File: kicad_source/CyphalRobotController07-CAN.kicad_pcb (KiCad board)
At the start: 2 copper layers, 140 x 70 mm, 177 parts, among them J1 BM04B-SRSS-TB, J10 x, J11 PowerPole, J12 Conn_01x02, J13 Conn_01x02, J14 Conn_01x02, J15 PinHeader_1x04, J16 PinHeader_1x04, J17 PinHeader_1x05, J18 Conn_01x02, J19 S6B-XH-A, J2 RASPBERRYPI_PICO, J20 S6B-XH-A, J3 BM04B-SRSS-TB, J4 B3B-PH-SM4-TB, J5 BM04B-GHS-TBT, J6 BM04B-GHS-TBT, J7 x, J8 x, J9 x, Q1 2N7002, Q2 IPD90P03P4L- 04, SW1 PTS636 SM43 SMTR LFS, U1 24LC64-I/SN, U10 ADS1015IDGS, U11 OPA2374AIDCN, U12 INA226, U13 IFX91041EFJ, U14 ITS4200S-ME-P, U15 ITS4200S-ME-P, U16 BNO085, U17 SN74LVC2T45DCUR, U18 SN74LVC2T45DCUR, U2 MCP2515-I/SO, U3 SN65HVD232, U4 74xx08, U5 IFX007T, U6 IFX007T, U7 IFX007T, U8 IFX007T, U9 OPA2374AIDCN, Y1 RH100-16.000-16-3030-EXT-TR, Y2 DNI

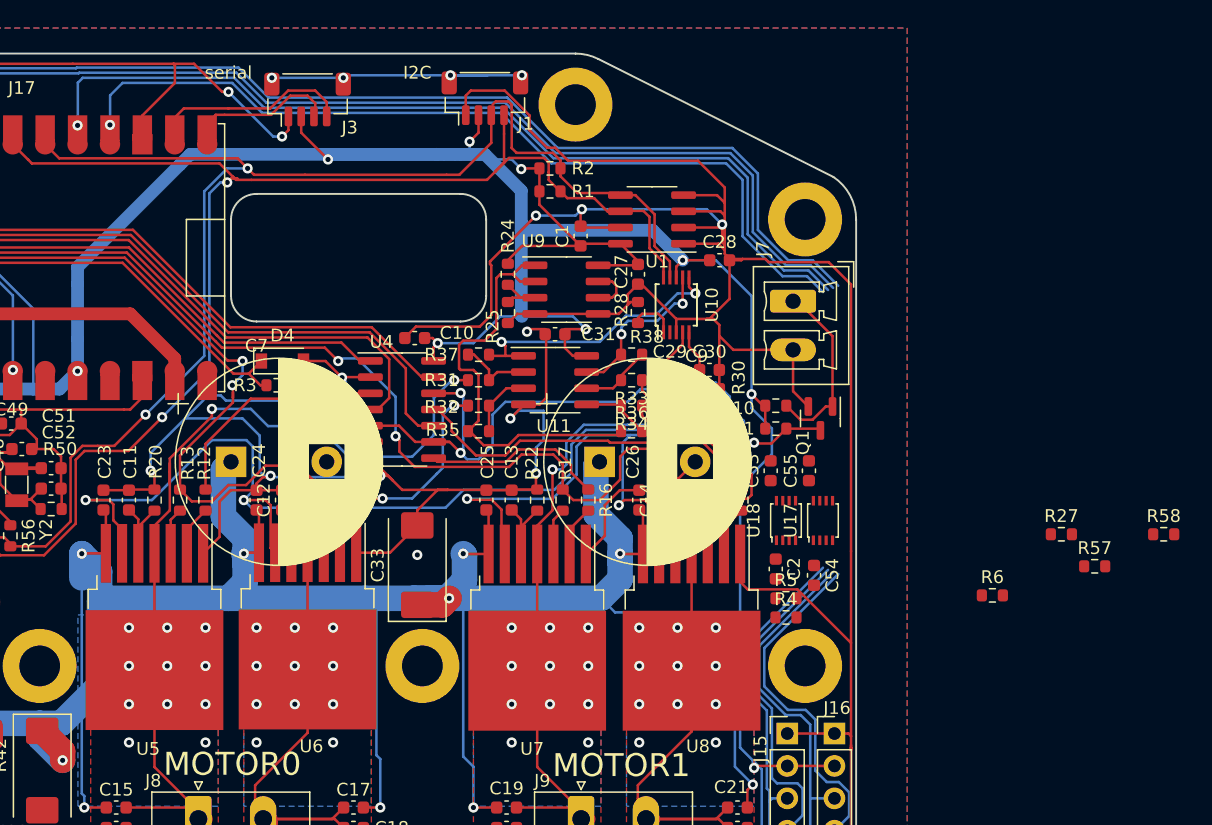
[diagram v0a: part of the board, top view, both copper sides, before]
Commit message: finished layout near encoder level converter
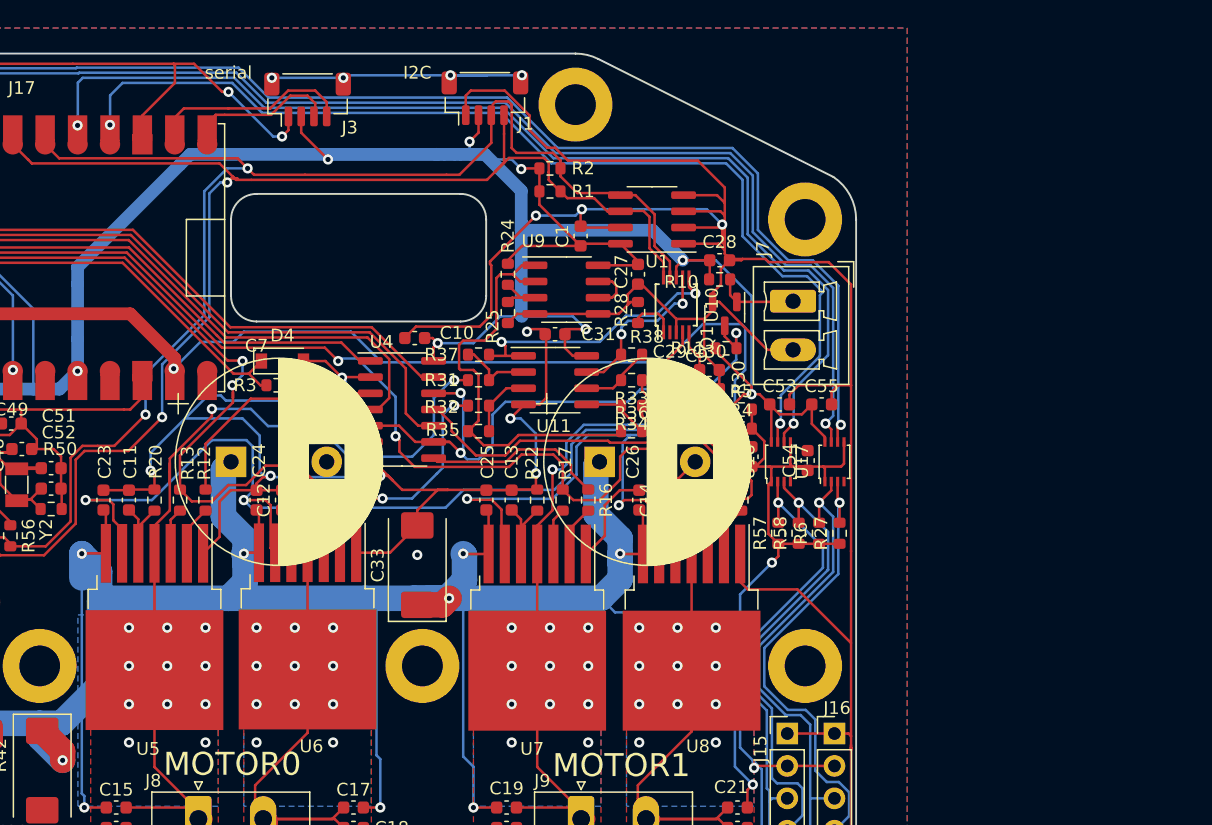
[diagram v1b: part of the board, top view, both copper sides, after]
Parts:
- moved R58 28.6 mm to (186.5, 93.6), turned to 90 degrees
- moved R57 24.9 mm to (184.9, 93.6), turned to 90 degrees
- moved R27 17.4 mm to (189.7, 93.6), turned to 90 degrees
- moved R4 15.2 mm to (182.0, 85.4)
- moved R5 15.2 mm to (182.0, 83.9)
- moved R6 14.4 mm to (188.1, 93.6), turned to 90 degrees
- moved Q1 11.1 mm to (180.7, 76.4)
- moved R10 10.8 mm to (180.3, 73.7)
- moved C54 9.01 mm to (187.2, 87.9), turned to 90 degrees
- moved C2 9.00 mm to (182.8, 87.6), turned to 90 degrees
- moved R11 7.41 mm to (180.8, 79.1)
- moved C55 5.30 mm to (188.3, 83.5), turned to 0 degrees
- moved C53 5.25 mm to (185.0, 83.5), turned to 0 degrees
- moved U17 4.69 mm to (189.3, 88.0)
- moved U18 4.62 mm to (185.1, 88.0)
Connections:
- C2 pad 1: Net-(J16-Pad2) -> VCOM
- C54 pad 1: Net-(J16-Pad2) -> VCOM
- J15 pad 2: Net-(J16-Pad2) -> VCOM
- J16 pad 2: Net-(J16-Pad2) -> VCOM
- J19 pad 4: +3.3V -> VCOM
- J20 pad 4: +3.3V -> VCOM
- R27 pad 1: Net-(J16-Pad2) -> VCOM
- R4 pad 2: Net-(J16-Pad2) -> VCOM
- R5 pad 2: Net-(J16-Pad2) -> VCOM
- R57 pad 1: Net-(J16-Pad2) -> VCOM
- R58 pad 1: Net-(J16-Pad2) -> VCOM
- R6 pad 1: Net-(J16-Pad2) -> VCOM
- U17 pad 1: Net-(J16-Pad2) -> VCOM
- U17 pad 5: Net-(J16-Pad2) -> VCOM
- U18 pad 1: Net-(J16-Pad2) -> VCOM
- U18 pad 5: Net-(J16-Pad2) -> VCOM
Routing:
- net VCOM: track 0.00 -> 104.8 mm, vias 0 -> 2
- net +3.3V: track 423.9 -> 354.4 mm, vias 14 -> 13
- net +5V: track 153.5 -> 212.4 mm, vias 2 -> 4
- net /QUAD3_U: track 72.0 -> 85.4 mm, vias 1 -> 2
- net /QUAD2_U: track 68.2 -> 81.5 mm, vias 1 -> 2
- net /QUAD1_U: track 111.7 -> 124.5 mm, vias 1 -> 2
- net /QUAD0_U: track 107.9 -> 120.5 mm, vias 1 -> 2
- net QUAD3: track 32.7 -> 42.7 mm, vias 0 -> 1
- net QUAD2: track 33.6 -> 43.4 mm, vias 0 -> 1
- net QUAD0: track 70.3 -> 79.8 mm, vias 0 -> 1
- net QUAD1: track 79.2 -> 88.1 mm, vias 0 -> 1
- net /MotorDriver/EM_STOP: track 14.2 -> 6.41 mm
- net /MotorDriver/EM_STOP_Q: track 63.6 -> 59.4 mm
- net GND: track 1071.6 -> 1073.1 mm

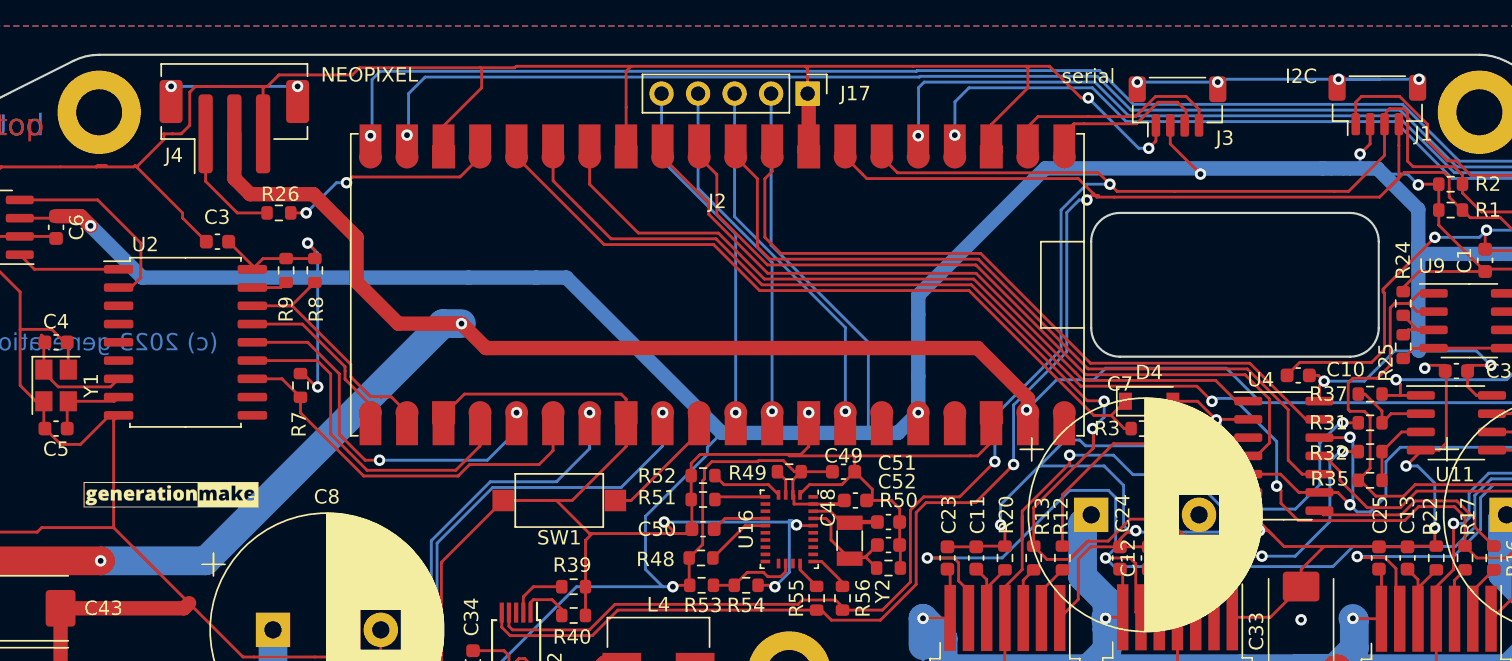
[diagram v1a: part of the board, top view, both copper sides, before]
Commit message: used raspberry pi pico with headers
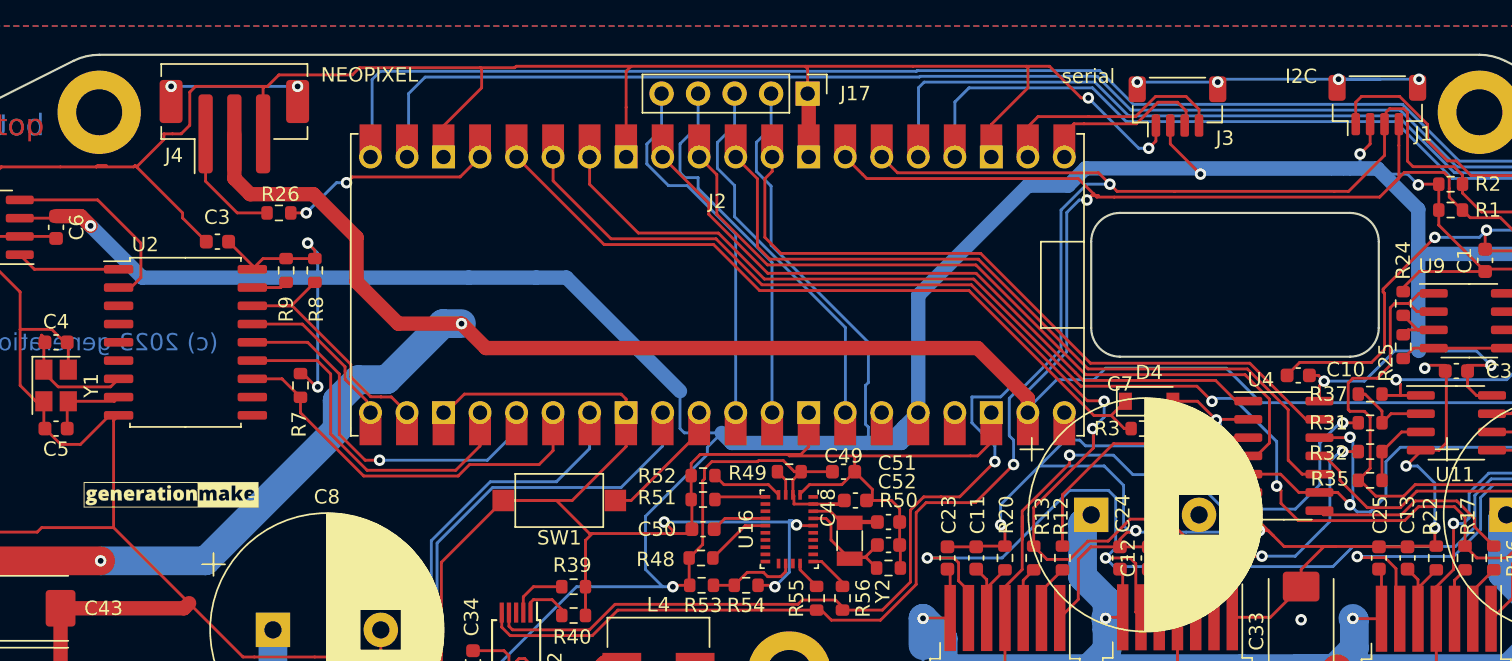
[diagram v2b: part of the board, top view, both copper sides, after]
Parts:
- J2: footprint generationmake:RASPI_PICO_SOLDER_Kopie -> generationmake:RASPI_PICO_SOLDER_NO_MOUNTING
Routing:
- net +3.3V: track 354.4 -> 359.5 mm, vias 13 -> 12
- net I2C_SDA: track 130.7 -> 133.7 mm
- net /QUAD2_U: track 81.5 -> 83.1 mm, vias 2 -> 1
- net /ANALOG_INPUT0: track 24.3 -> 25.9 mm, vias 1 -> 0
- net /QUAD3_U: track 85.4 -> 87.0 mm, vias 2 -> 1
- net /ANALOG_INPUT1: track 24.2 -> 25.8 mm, vias 1 -> 0
- net /QUAD0_U: track 120.5 -> 122.0 mm, vias 2 -> 1
- net /QUAD1_U: track 124.5 -> 126.0 mm, vias 2 -> 1
- net +5V: track 212.4 -> 213.6 mm, vias 4 -> 3
- net /ANALOG_INPUT2: track 25.3 -> 26.3 mm, vias 1 -> 0
- net I2C_SCL: track 131.9 -> 132.6 mm
- net OUTPUT1: vias 2 -> 1
- net OUTPUT0: vias 2 -> 1
- net MOSI: vias 2 -> 1
- net GND: vias 17 -> 16

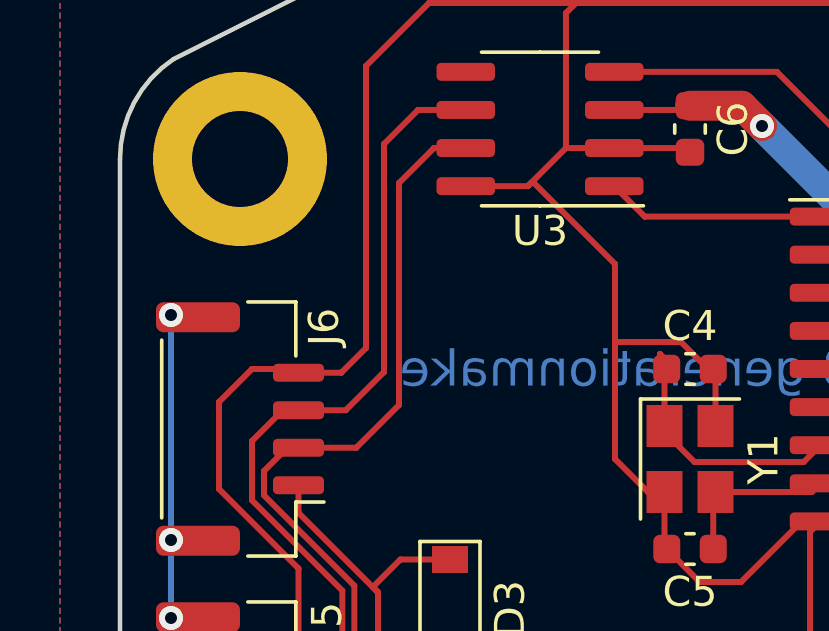
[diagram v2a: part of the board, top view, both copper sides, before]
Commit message: added protection on CAN
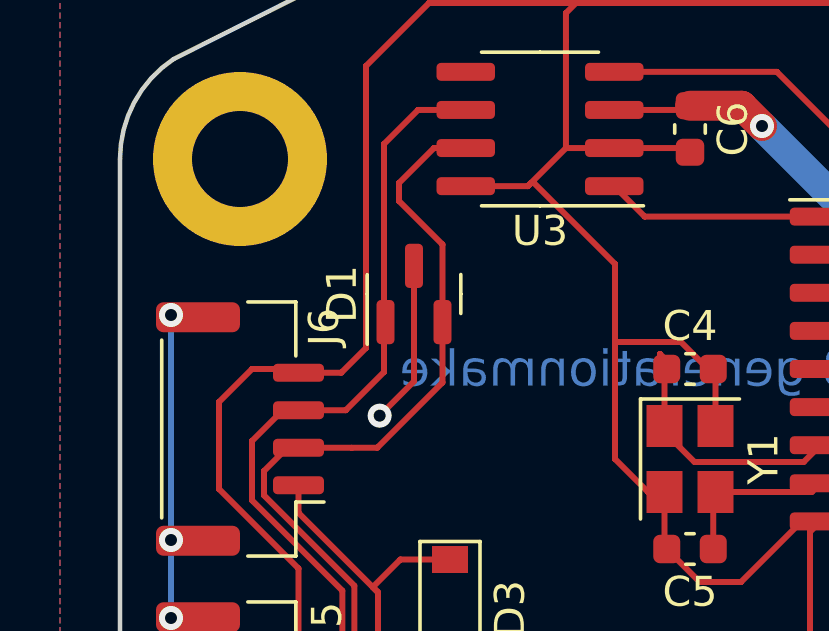
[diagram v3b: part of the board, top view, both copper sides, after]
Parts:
- added D1: NUP2105L, Package_TO_SOT_SMD:SOT-23, F.Cu at (60.8, 73.5)
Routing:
- net GND: track 1073.1 -> 1078.6 mm, vias 16 -> 17
- net /MCP2515/CANH: track 27.5 -> 29.1 mm
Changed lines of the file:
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@@
     )
   )
+  (footprint "Package_TO_SOT_SMD:SOT-23" (layer "F.Cu")
+    (at 60.8 73.5 90)
+    (descr "SOT, 3 Pin (https://www.jedec.org/system/files/docs/to-236h.pdf variant AB), generated with kicad-footprint-generator ipc_gullwing_generator.py")
+    (tags "SOT TO_SOT_SMD")
+    (property "Sheetfile" "mcp2515.kicad_sch")
+    (property "Sheetname" "MCP2515")
+    (attr smd)
+    (fp_text reference "D1" (at 0 -2.4 90) (layer "F.SilkS")
+      (effects (font (size 1 1) (thickness 0.15)))
+    )
+    (fp_text value "NUP2105L" (at 0 2.4 90) (layer "F.Fab")
+      (effects (font (size 1 1) (thickness 0.15)))
+    )
+    (fp_text user "${REFERENCE}" (at 0 0 90) (layer "F.Fab")
+      (effects (font (size 0.32 0.32) (thickness 0.05)))
+    )
+    (fp_line (start 0 -1.56) (end -1.675 -1.56) (layer "F.SilkS") (width 0.12))
+    (fp_line (start 0 -1.56) (end 0.65 -1.56) (layer "F.SilkS") (width 0.12))
+    (fp_line (start 0 1.56) (end 0.65 1.56) (layer "F.SilkS") (width 0.12))
+    (fp_line (start 0 1.56) (end -0.65 1.56) (layer "F.SilkS") (width 0.12))
+    (fp_line (start 1.92 1.7) (end 1.92 -1.7) (layer "F.CrtYd") (width 0.05))
+    (fp_line (start -1.92 -1.7) (end -1.92 1.7) (layer "F.CrtYd") (width 0.05))
+    (fp_line (start -1.92 1.7) (end 1.92 1.7) (layer "F.CrtYd") (width 0.05))
+    (fp_line (start 1.92 -1.7) (end -1.92 -1.7) (layer "F.CrtYd") (width 0.05))
+    (fp_line (start -0.65 1.45) (end -0.65 -1.125) (layer "F.Fab") (width 0.1))
+    (fp_line (start -0.65 -1.125) (end -0.325 -1.45) (layer "F.Fab") (width 0.1))
+    (fp_line (start 0.65 1.45) (end -0.65 1.45) (layer "F.Fab") (width 0.1))
+    (fp_line (start -0.325 -1.45) (end 0.65 -1.45) (layer "F.Fab") (width 0.1))
+    (fp_line (start 0.65 -1.45) (end 0.65 1.45) (layer "F.Fab") (width 0.1))
+    (pad "1" smd roundrect (at -0.9375 -0.95 90) (size 1.475 0.6) (layers "F.Cu" "F.Paste" "F.Mask") (roundrect_rratio 0.25)
+      (net 68 "/MCP2515/CANL") (pinfunction "K") (pintype "passive"))
+    (pad "2" smd roundrect (at -0.9375 0.95 90) (size 1.475 0.6) (layers "F.Cu" "F.Paste" "F.Mask") (roundrect_rratio 0.25)
+      (net 67 "/MCP2515/CANH") (pinfunction "K") (pintype "passive"))
+    (pad "3" smd roundrect (at 0.9375 0 90) (size 1.475 0.6) (layers "F.Cu" "F.Paste" "F.Mask") (roundrect_rratio 0.25)
+      (net 1 "GND") (pinfunction "A") (pintype "passive"))
+    (model "${KICAD6_3DMODEL_DIR}/Package_TO_SOT_SMD.3dshapes/SOT-23.wrl"
+      (offset (xyz 0 0 0))
+      (scale (xyz 1 1 1))
+      (rotate (xyz 0 0 0))
+    )
+  )
   (footprint "Capacitor_SMD:C_0603_1608Metric" (layer "F.Cu")
     (at 125.6 87)
@@
   (segment (start 85.41 123.69) (end 83.0775 121.3575) (width 0.2) (layer "F.Cu") (net 1))
   (segment (start 174.175 74.075) (end 175.2 75.1) (width 0.2) (layer "F.Cu") (net 1))
+  (segment (start 60.8 76) (end 60.8 76.410756) (width 0.2) (layer "F.Cu") (net 1))
   (segment (start 70.775 76) (end 70.6 76) (width 0.2) (layer "F.Cu") (net 1))
   (segment (start 161.7 116.7) (end 161.225 117.175) (width 0.2) (layer "F.Cu") (net 1))
@@
   (segment (start 161.99 90.2) (end 159 90.2) (width 0.2) (layer "F.Cu") (net 1))
   (segment (start 61.095 120.87) (end 61.225 121) (width 0.2) (layer "F.Cu") (net 1))
+  (segment (start 60.8 72.5625) (end 60.8 76) (width 0.2) (layer "F.Cu") (net 1))
   (segment (start 58.2 93) (end 60.25 90.95) (width 0.2) (layer "F.Cu") (net 1))
   (segment (start 53.5 104.4) (end 52.8 103.7) (width 0.2) (layer "F.Cu") (net 1))
@@
   (segment (start 79.25625 94.14375) (end 74 88.8875) (width 0.2) (layer "F.Cu") (net 1))
   (segment (start 180.7 66.5) (end 178.6 64.4) (width 0.2) (layer "F.Cu") (net 1))
+  (segment (start 60.8 76.410756) (end 59.655378 77.555378) (width 0.2) (layer "F.Cu") (net 1))
   (segment (start 130.7125 123.7125) (end 131.225 123.2) (width 1) (layer "F.Cu") (net 1))
   (segment (start 122.4 85.9) (end 124.65 85.9) (width 0.2) (layer "F.Cu") (net 1))
@@
   (via (at 141.8 59) (size 0.8) (drill 0.4) (layers "F.Cu" "B.Cu") (net 1))
   (via (at 147.9 82) (size 0.8) (drill 0.4) (layers "F.Cu" "B.Cu") (net 1))
+  (via (at 59.655378 77.555378) (size 0.8) (drill 0.4) (layers "F.Cu" "B.Cu") (net 1))
   (via (at 135.7 88.7) (size 0.8) (drill 0.4) (layers "F.Cu" "B.Cu") (net 1))
   (via (at 169.5 68.2) (size 0.8) (drill 0.4) (layers "F.Cu" "B.Cu") (net 1))
@@
   (segment (start 55.8 79.4) (end 55.8 80.211396) (width 0.2) (layer "F.Cu") (net 67))
   (segment (start 62.525 68.635) (end 61.465 68.635) (width 0.2) (layer "F.Cu") (net 67))
+  (segment (start 61.75 71.85) (end 61.75 74.4375) (width 0.2) (layer "F.Cu") (net 67))
+  (segment (start 59.575 78.625) (end 58.725 78.625) (width 0.2) (layer "F.Cu") (net 67))
   (segment (start 56.95 78.625) (end 56.575 78.625) (width 0.2) (layer "F.Cu") (net 67))
+  (segment (start 60.3 70.1) (end 60.3 70.4) (width 0.2) (layer "F.Cu") (net 67))
   (segment (start 58.811459 88.038541) (end 58.225 88.625) (width 0.2) (layer "F.Cu") (net 67))
+  (segment (start 61.75 76.45) (end 59.575 78.625) (width 0.2) (layer "F.Cu") (net 67))
+  (segment (start 61.75 74.4375) (end 61.75 76.45) (width 0.2) (layer "F.Cu") (net 67))
+  (segment (start 60.3 70.1) (end 60.3 69.8) (width 0.2) (layer "F.Cu") (net 67))
   (segment (start 58.225 88.625) (end 56.95 88.625) (width 0.2) (layer "F.Cu") (net 67))
-  (segment (start 58.875 78.625) (end 56.95 78.625) (width 0.2) (layer "F.Cu") (net 67))
-  (segment (start 60.3 77) (end 60.3 77.2) (width 0.2) (layer "F.Cu") (net 67))
-  (segment (start 60.3 77) (end 60.3 69.8) (width 0.2) (layer "F.Cu") (net 67))
+  (segment (start 58.725 78.625) (end 56.95 78.625) (width 0.2) (layer "F.Cu") (net 67))
+  (segment (start 60.3 70.4) (end 61.75 71.85) (width 0.2) (layer "F.Cu") (net 67))
   (segment (start 60.3 69.8) (end 61.465 68.635) (width 0.2) (layer "F.Cu") (net 67))
-  (segment (start 60.3 77.2) (end 58.875 78.625) (width 0.2) (layer "F.Cu") (net 67))
   (segment (start 55.8 80.211396) (end 58.811459 83.222856) (width 0.2) (layer "F.Cu") (net 67))
   (segment (start 58.811459 83.222856) (end 58.811459 88.038541) (width 0.2) (layer "F.Cu") (net 67))
